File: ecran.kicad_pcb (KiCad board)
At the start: 4 copper layers, 43 x 43 mm, 15 parts, among them J6 MEC1-110-02-F-D-A, J8 MEC1-110-02-F-D-A, SW1 RotaryEncoder_Switch_MP

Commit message: maj puissance
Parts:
- moved C12 43.0 mm to (128.1, 105.5)
- moved C13 43.0 mm to (108.9, 126.9)
- moved C14 43.0 mm to (106.2, 124.2)
- moved C15 43.0 mm to (106.2, 118.8)
- moved J6 43.0 mm to (114.0, 114.0)
- moved J8 43.0 mm to (137.0, 116.0)
- moved R11 43.0 mm to (115.4, 105.5)
- moved R12 43.0 mm to (117.9, 105.5)
- moved R13 43.0 mm to (120.5, 105.5)
- moved R14 43.0 mm to (123.1, 105.5)
- moved R16 43.0 mm to (132.1, 133.0)
- moved R17 43.0 mm to (110.9, 133.0)
- moved R18 43.0 mm to (110.9, 138.0)
- moved SW1 43.0 mm to (121.5, 135.5)
- moved U8 43.0 mm to (121.5, 115.7)
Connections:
- net Net-(J6-Pad06) renamed +5V
- J6 pad 02: Net-(J6-Pad02) -> +3.3V
- J6 pad 04: Net-(J6-Pad04) -> GND1
- J6 pad 08: Net-(J6-Pad08) -> /OUTPUT_4
- J6 pad 10: Net-(J6-Pad10) -> /OUTPUT_6
- J6 pad 12: Net-(J6-Pad12) -> /OUTPUT_5
- J6 pad 16: Net-(J6-Pad16) -> /OUTPUT_3
- J6 pad 18: Net-(J6-Pad18) -> /OUTPUT_2
- J6 pad 20: Net-(J6-Pad20) -> /OUTPUT_1
- J8 pad 01: Net-(J6-Pad02) -> +3.3V
- J8 pad 02: Net-(J6-Pad02) -> +3.3V
- J8 pad 03: Net-(J6-Pad04) -> GND1
- J8 pad 04: Net-(J6-Pad04) -> GND1
- J8 pad 07: Net-(J6-Pad08) -> /OUTPUT_4
- J8 pad 08: Net-(J6-Pad08) -> unconnected-(J8-Pad08)
- J8 pad 09: Net-(J6-Pad10) -> /OUTPUT_6
- J8 pad 10: Net-(J6-Pad10) -> unconnected-(J8-Pad10)
- J8 pad 11: Net-(J6-Pad12) -> /OUTPUT_5
- J8 pad 12: Net-(J6-Pad12) -> unconnected-(J8-Pad12)
- J8 pad 15: Net-(J6-Pad16) -> /OUTPUT_3
- J8 pad 16: Net-(J6-Pad16) -> unconnected-(J8-Pad16)
- J8 pad 17: Net-(J6-Pad18) -> /OUTPUT_2
- J8 pad 18: Net-(J6-Pad18) -> unconnected-(J8-Pad18)
- J8 pad 19: Net-(J6-Pad20) -> /OUTPUT_1
- J8 pad 20: Net-(J6-Pad20) -> unconnected-(J8-Pad20)
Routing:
- net +3.3V: track 8.47 -> 141.9 mm
- net Net-(J6-Pad20): track 25.8 -> 0.00 mm
- net Net-(J6-Pad18): track 25.8 -> 0.00 mm
- net Net-(J6-Pad16): track 25.8 -> 0.00 mm
- net Net-(J6-Pad12): track 25.8 -> 0.00 mm
- net Net-(J6-Pad10): track 25.8 -> 0.00 mm
- net Net-(J6-Pad08): track 25.8 -> 0.00 mm
- net Net-(J6-Pad04): track 25.8 -> 0.00 mm
- net Net-(J6-Pad02): track 25.8 -> 0.00 mm
- net /OUTPUT_6: track 0.00 -> 16.8 mm
- net /OUTPUT_5: track 0.00 -> 16.8 mm
- net /OUTPUT_4: track 0.00 -> 16.8 mm
- net /OUTPUT_3: track 0.00 -> 16.8 mm
- net /OUTPUT_2: track 0.00 -> 16.8 mm
- net /OUTPUT_1: track 0.00 -> 16.8 mm
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- added copper zone on B.Cu, net GND1
- removed copper zone on In1.Cu, net +3.3V
- removed copper zone on In2.Cu, net GND1
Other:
- copper layers 4 -> 2

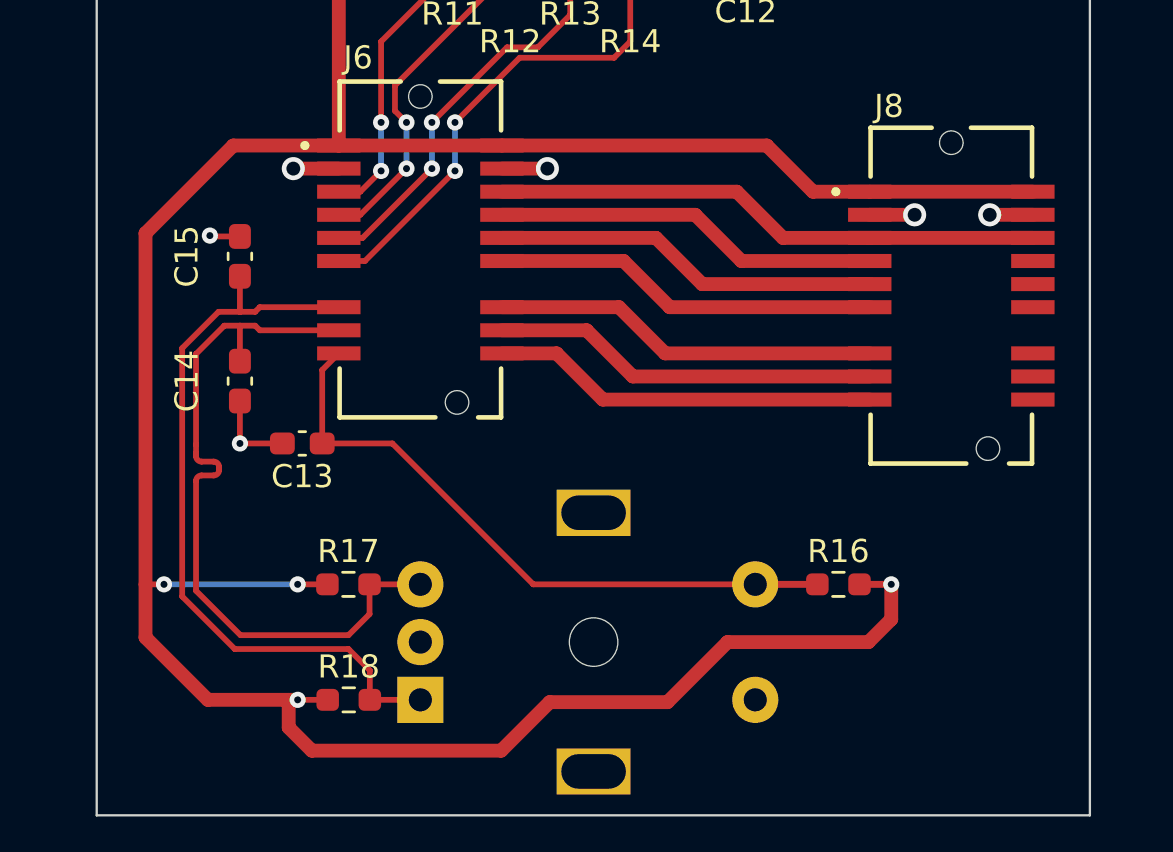
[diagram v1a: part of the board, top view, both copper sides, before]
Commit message: découpage et hierarchie
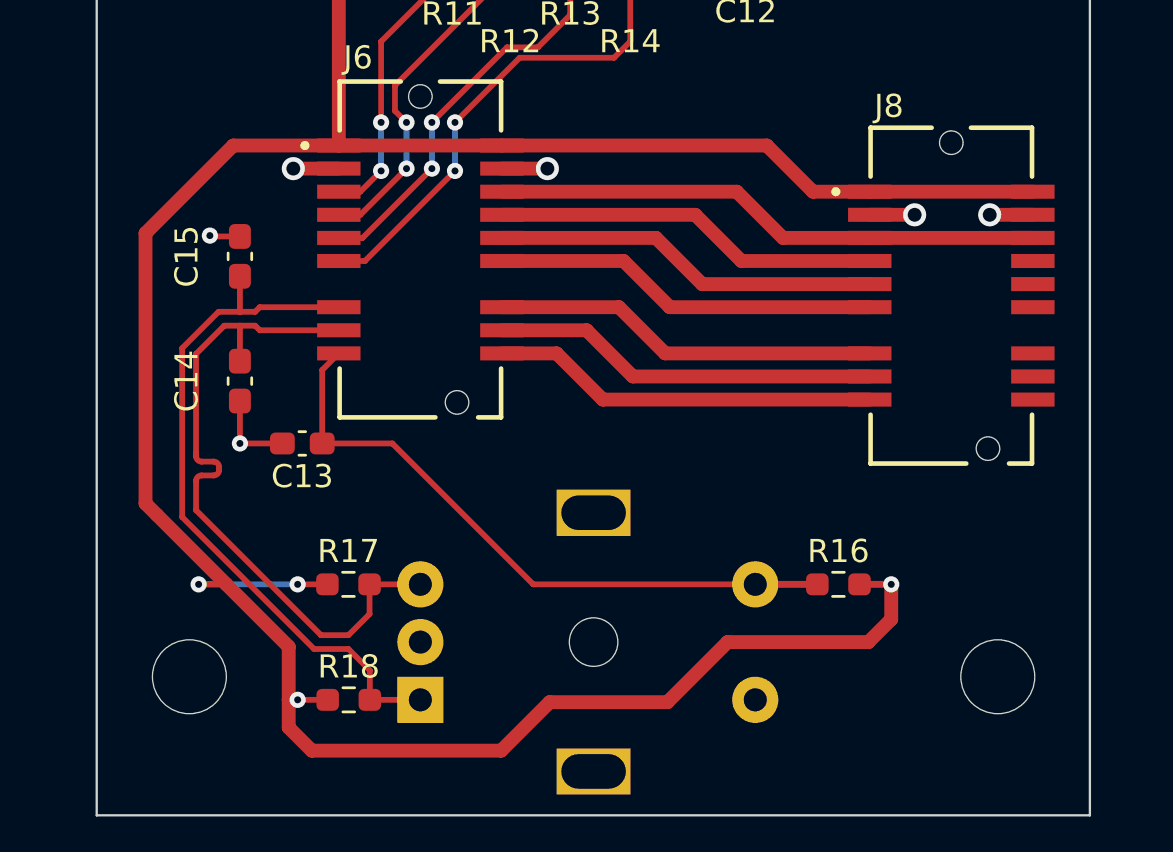
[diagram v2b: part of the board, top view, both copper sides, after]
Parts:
- added REF**: MountingHole_3.2mm_M3, MountingHole:MountingHole_3.2mm_M3, F.Cu at (139.0, 137.0)
- added REF**: MountingHole_3.2mm_M3, MountingHole:MountingHole_3.2mm_M3, F.Cu at (104.0, 137.0)
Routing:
- net +3.3V: track 141.9 -> 139.2 mm
- net /ROTENC_-: track 32.3 -> 30.2 mm
- net /ROTENC_+: track 32.8 -> 30.8 mm

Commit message: assemblage 3d
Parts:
- removed REF** (x2): MountingHole_3.2mm_M3, MountingHole:MountingHole_3.2mm_M3
- added H1: MountingHole, MountingHole:MountingHole_3.2mm_M3_DIN965, F.Cu at (104.0, 137.0)
- added H2: MountingHole, MountingHole:MountingHole_3.2mm_M3_DIN965, F.Cu at (139.0, 137.0)
- moved J8 7.99 mm to (129.0, 116.0)
- moved J6 1.00 mm to (115.0, 114.0)
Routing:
- net +3.3V: track 139.2 -> 128.8 mm, vias 4 -> 2
- net +5V: track 23.8 -> 14.8 mm
- net /OUTPUT_6: track 16.8 -> 7.77 mm
- net /OUTPUT_5: track 16.8 -> 7.77 mm
- net /OUTPUT_4: track 16.8 -> 7.77 mm
- net /OUTPUT_3: track 16.8 -> 7.77 mm
- net /OUTPUT_2: track 16.8 -> 7.77 mm
- net /OUTPUT_1: track 16.8 -> 7.77 mm
- net Net-(J6-Pad11): track 20.9 -> 18.1 mm
- net Net-(J6-Pad09): track 17.1 -> 15.9 mm

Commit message: suite et nouvel écran
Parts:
- SW1: value RotaryEncoder_Switch_MP -> PEC11L-4220K-S0015
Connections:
- net Net-(J6-Pad05) renamed /LCD_DIN
- net Net-(J6-Pad07) renamed /LCD_CLK
- net Net-(J6-Pad09) renamed /LCD_CS
- net Net-(J6-Pad11) renamed /LCD_DC
- J8 pad 08: unconnected-(J8-Pad08) -> /OUTPUT_4
- J8 pad 10: unconnected-(J8-Pad10) -> /OUTPUT_6
- J8 pad 12: unconnected-(J8-Pad12) -> /OUTPUT_5
- J8 pad 16: unconnected-(J8-Pad16) -> /OUTPUT_3
- J8 pad 18: unconnected-(J8-Pad18) -> /OUTPUT_2
- J8 pad 20: unconnected-(J8-Pad20) -> /OUTPUT_1
- U8 pad 7: +3.3V -> GND1
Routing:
- net /OUTPUT_6: track 7.77 -> 14.8 mm
- net /OUTPUT_5: track 7.77 -> 14.8 mm
- net /OUTPUT_4: track 7.77 -> 14.8 mm
- net /OUTPUT_3: track 7.77 -> 14.8 mm
- net /OUTPUT_2: track 7.77 -> 14.8 mm
- net /OUTPUT_1: track 7.77 -> 14.8 mm
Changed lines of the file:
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@@
 			(size 0.61 1.88)
 			(layers "F.Cu" "F.Mask" "F.Paste")
-			(net "unconnected-(J8-Pad08)")
+			(net "/OUTPUT_4")
 			(pinfunction "08_08")
 			(pintype "passive")
@@
 			(size 0.61 1.88)
 			(layers "F.Cu" "F.Mask" "F.Paste")
-			(net "unconnected-(J8-Pad10)")
+			(net "/OUTPUT_6")
 			(pinfunction "10_10")
 			(pintype "passive")
@@
 			(size 0.61 1.88)
 			(layers "F.Cu" "F.Mask" "F.Paste")
-			(net "unconnected-(J8-Pad12)")
+			(net "/OUTPUT_5")
 			(pinfunction "12_12")
 			(pintype "passive")
@@
 			(size 0.61 1.88)
 			(layers "F.Cu" "F.Mask" "F.Paste")
-			(net "unconnected-(J8-Pad16)")
+			(net "/OUTPUT_3")
 			(pinfunction "16_16")
 			(pintype "passive")
@@
 			(size 0.61 1.88)
 			(layers "F.Cu" "F.Mask" "F.Paste")
-			(net "unconnected-(J8-Pad18)")
+			(net "/OUTPUT_2")
 			(pinfunction "18_18")
 			(pintype "passive")
@@
 			(size 0.61 1.88)
 			(layers "F.Cu" "F.Mask" "F.Paste")
-			(net "unconnected-(J8-Pad20)")
+			(net "/OUTPUT_1")
 			(pinfunction "20_20")
 			(pintype "passive")
@@
 			(layers "F.Cu" "F.Mask" "F.Paste")
 			(roundrect_rratio 0.25)
-			(net "Net-(J6-Pad07)")
+			(net "/LCD_CLK")
 			(pintype "passive")
 		)
@@
 			(layers "F.Cu" "F.Mask" "F.Paste")
 			(roundrect_rratio 0.25)
-			(net "Net-(J6-Pad11)")
+			(net "/LCD_DC")
 			(pintype "passive")
 		)
@@
 			(layers "F.Cu" "F.Mask" "F.Paste")
 			(roundrect_rratio 0.25)
-			(net "Net-(J6-Pad05)")
+			(net "/LCD_DIN")
 			(pintype "passive")
 		)
@@
 			(size 0.61 1.88)
 			(layers "F.Cu" "F.Mask" "F.Paste")
-			(net "Net-(J6-Pad05)")
+			(net "/LCD_DIN")
 			(pinfunction "05_05")
 			(pintype "passive")
@@
 			(size 0.61 1.88)
 			(layers "F.Cu" "F.Mask" "F.Paste")
-			(net "Net-(J6-Pad07)")
+			(net "/LCD_CLK")
 			(pinfunction "07_07")
 			(pintype "passive")
@@
 			(size 0.61 1.88)
 			(layers "F.Cu" "F.Mask" "F.Paste")
-			(net "Net-(J6-Pad09)")
+			(net "/LCD_CS")
 			(pinfunction "09_09")
 			(pintype "passive")
@@
 			(size 0.61 1.88)
 			(layers "F.Cu" "F.Mask" "F.Paste")
-			(net "Net-(J6-Pad11)")
+			(net "/LCD_DC")
 			(pinfunction "11_11")
 			(pintype "passive")
@@
 			(layers "F.Cu" "F.Mask" "F.Paste")
 			(roundrect_rratio 0.25)
-			(net "Net-(J6-Pad09)")
+			(net "/LCD_CS")
 			(pintype "passive")
 		)
@@
 			(layers "*.Cu" "*.Mask")
 			(remove_unused_layers no)
-			(net "+3.3V")
+			(net "GND1")
 			(pinfunction "RST_7")
 			(pintype "input")
@@
 			)
 		)
-		(property "Value" "RotaryEncoder_Switch_MP"
+		(property "Value" "PEC11L-4220K-S0015"
 			(at 0 -7.9 0)
 			(unlocked yes)
@@
 	)
 	(segment
+		(start 125.4695 119)
+		(end 132.5305 119)
+		(width 0.6)
+		(layer "F.Cu")
+		(net "/OUTPUT_4")
+	)
+	(segment
 		(start 121.9 117)
 		(end 123.9 119)
@@
 	)
 	(segment
+		(start 125.4695 120)
+		(end 132.5305 120)
+		(width 0.6)
+		(layer "F.Cu")
+		(net "/OUTPUT_6")
+	)
+	(segment
 		(start 123.6 120)
 		(end 121.6 118)
@@
 	)
 	(segment
+		(start 125.4695 121)
+		(end 132.5305 121)
+		(width 0.6)
+		(layer "F.Cu")
+		(net "/OUTPUT_5")
+	)
+	(segment
 		(start 121.4 119)
 		(end 118.5305 119)
@@
 	)
 	(segment
+		(start 125.4695 123)
+		(end 132.5305 123)
+		(width 0.6)
+		(layer "F.Cu")
+		(net "/OUTPUT_3")
+	)
+	(segment
 		(start 123.6 123)
 		(end 121.6 121)
@@
 	)
 	(segment
+		(start 125.4695 124)
+		(end 132.5305 124)
+		(width 0.6)
+		(layer "F.Cu")
+		(net "/OUTPUT_2")
+	)
+	(segment
 		(start 121.3 122)
 		(end 118.5305 122)
@@
 	)
 	(segment
+		(start 125.4695 125)
+		(end 132.5305 125)
+		(width 0.6)
+		(layer "F.Cu")
+		(net "/OUTPUT_1")
+	)
+	(segment
 		(start 122.9 125)
 		(end 120.9 123)
@@
 		(width 0.25)
 		(layer "F.Cu")
-		(net "Net-(J6-Pad07)")
+		(net "/LCD_CLK")
 	)
 	(segment
@@
 		(width 0.25)
 		(layer "F.Cu")
-		(net "Net-(J6-Pad07)")
+		(net "/LCD_CLK")
 	)
 	(segment
@@
 		(width 0.25)
 		(layer "F.Cu")
-		(net "Net-(J6-Pad07)")
+		(net "/LCD_CLK")
 	)
 	(segment
@@
 		(width 0.25)
 		(layer "F.Cu")
-		(net "Net-(J6-Pad07)")
+		(net "/LCD_CLK")
 	)
 	(segment
@@
 		(width 0.25)
 		(layer "F.Cu")
-		(net "Net-(J6-Pad07)")
+		(net "/LCD_CLK")
 	)
 	(segment
@@
 		(width 0.25)
 		(layer "F.Cu")
-		(net "Net-(J6-Pad07)")
+		(net "/LCD_CLK")
 	)
 	(via
@@
 		(drill 0.3)
 		(layers "F.Cu" "B.Cu")
-		(net "Net-(J6-Pad07)")
+		(net "/LCD_CLK")
 	)
 	(via
@@
 		(drill 0.3)
 		(layers "F.Cu" "B.Cu")
-		(net "Net-(J6-Pad07)")
+		(net "/LCD_CLK")
 	)
 	(segment
@@
 		(width 0.25)
 		(layer "B.Cu")
-		(net "Net-(J6-Pad07)")
+		(net "/LCD_CLK")
 	)
 	(segment
@@
 		(width 0.25)
 		(layer "F.Cu")
-		(net "Net-(J6-Pad11)")
+		(net "/LCD_DC")
 	)
 	(segment
@@
 		(width 0.25)
 		(layer "F.Cu")
-		(net "Net-(J6-Pad11)")
+		(net "/LCD_DC")
 	)
 	(segment
@@
 		(width 0.25)
 		(layer "F.Cu")
-		(net "Net-(J6-Pad11)")
+		(net "/LCD_DC")
 	)
 	(via
@@
 		(drill 0.3)
 		(layers "F.Cu" "B.Cu")
-		(net "Net-(J6-Pad11)")
+		(net "/LCD_DC")
 	)
 	(via
@@
 		(drill 0.3)
 		(layers "F.Cu" "B.Cu")
-		(net "Net-(J6-Pad11)")
+		(net "/LCD_DC")
 	)
 	(segment
@@
 		(width 0.25)
 		(layer "B.Cu")
-		(net "Net-(J6-Pad11)")
+		(net "/LCD_DC")
 	)
 	(segment
@@
 		(width 0.25)
 		(layer "F.Cu")
-		(net "Net-(J6-Pad05)")
+		(net "/LCD_DIN")
 	)
 	(segment
@@
 		(width 0.25)
 		(layer "F.Cu")
-		(net "Net-(J6-Pad05)")
+		(net "/LCD_DIN")
 	)
 	(segment
@@
 		(width 0.25)
 		(layer "F.Cu")
-		(net "Net-(J6-Pad05)")
+		(net "/LCD_DIN")
 	)
 	(segment
@@
 		(width 0.25)
 		(layer "F.Cu")
-		(net "Net-(J6-Pad05)")
+		(net "/LCD_DIN")
 	)
 	(segment
@@
 		(width 0.25)
 		(layer "F.Cu")
-		(net "Net-(J6-Pad05)")
+		(net "/LCD_DIN")
 	)
 	(via
@@
 		(drill 0.3)
 		(layers "F.Cu" "B.Cu")
-		(net "Net-(J6-Pad05)")
+		(net "/LCD_DIN")
 	)
 	(via
@@
 		(drill 0.3)
 		(layers "F.Cu" "B.Cu")
-		(net "Net-(J6-Pad05)")
+		(net "/LCD_DIN")
 	)
 	(segment
@@
 		(width 0.25)
 		(layer "B.Cu")
-		(net "Net-(J6-Pad05)")
+		(net "/LCD_DIN")
 	)
 	(segment
@@
 		(width 0.25)
 		(layer "F.Cu")
-		(net "Net-(J6-Pad09)")
+		(net "/LCD_CS")
 	)
 	(segment
@@
 		(width 0.25)
 		(layer "F.Cu")
-		(net "Net-(J6-Pad09)")
+		(net "/LCD_CS")
 	)
 	(segment
@@
 		(width 0.25)
 		(layer "F.Cu")
-		(net "Net-(J6-Pad09)")
+		(net "/LCD_CS")
 	)
 	(segment
@@
 		(width 0.25)
 		(layer "F.Cu")
-		(net "Net-(J6-Pad09)")
+		(net "/LCD_CS")
 	)
 	(via
@@
 		(drill 0.3)
 		(layers "F.Cu" "B.Cu")
-		(net "Net-(J6-Pad09)")
+		(net "/LCD_CS")
 	)
 	(via
@@
 		(drill 0.3)
 		(layers "F.Cu" "B.Cu")
-		(net "Net-(J6-Pad09)")
+		(net "/LCD_CS")
 	)
 	(segment
@@
 		(width 0.25)
 		(layer "B.Cu")
-		(net "Net-(J6-Pad09)")
+		(net "/LCD_CS")
 	)
 	(segment
